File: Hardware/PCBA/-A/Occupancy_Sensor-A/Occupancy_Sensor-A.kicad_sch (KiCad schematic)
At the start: 60 parts, among them J1 USB_C_Receptacle, J2 Conn_02x05_Odd_Even, Q1 2N7002, Q2 2N7002, SW1 SW_Push, SW2 SW_SPDT, U1 TPS78318DDCR, U3 TPS562200, U4 STM32WB55CGUx, U6 ECMF02-2AMX6, Y1 Crystal_GND24_Small, Y2 Crystal_GND24_Small

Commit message: Start layout, component fixes
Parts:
- C1, C10, C11, C12, C13, C14, C15, C16, C17, C18, C19, C2, C20, C21, C22, C23, C24, C25, C3, C4, C5, C6, C7, C8, C9: footprint (none) -> Capacitor_SMD:C_0402_1005Metric
- D2, D3: footprint (none) -> LED_SMD:LED_0603_1608Metric
- J1: footprint (none) -> Connector_USB:USB_C_Receptacle_Molex_105450-0101
- J2: footprint (none) -> Connector_PinHeader_1.27mm:PinHeader_2x05_P1.27mm_Vertical_SMD
- JP1: footprint (none) -> Jumper:SolderJumper-2_P1.3mm_Open_TrianglePad1.0x1.5mm
- L1: footprint (none) -> Inductor_SMD:L_0805_2012Metric
- L2: footprint (none) -> Inductor_SMD:L_Sumida_CDMC6D28_7.25x6.5mm
- L3: footprint (none) -> Inductor_SMD:L_0402_1005Metric
- R1, R2, R3, R4: footprint (none) -> Resistor_SMD:R_0402_1005Metric
- R10, R11, R12, R13, R14, R15, R6, R9: renamed from R5; footprint (none) -> Resistor_SMD:R_0402_1005Metric
- R5: renamed from R8; footprint (none) -> Resistor_SMD:R_0402_1005Metric
- R7: renamed from R6; footprint (none) -> Resistor_SMD:R_0402_1005Metric
- R8: renamed from R7; footprint (none) -> Resistor_SMD:R_0402_1005Metric
- SW1: footprint (none) -> Button_Switch_SMD:SW_Push_SPST_NO_Alps_SKRK
- SW2: footprint (none) -> Button_Switch_SMD:SW_SPDT_CK-JS102011SAQN
- U1: footprint TPS78318DDCR:SOT95P280X110-5N -> Package_TO_SOT_SMD:SOT-23-5
- U2: footprint (none) -> Occupancy_Sensor_Custom_Footprints:TCS3430
- Y1, Y2: footprint (none) -> Crystal:Crystal_SMD_SeikoEpson_FA128-4Pin_2.0x1.6mm
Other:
- moved on the sheet: C1, C10, C11, C12, C13, C14, C15, C16, C18, C19, C2, C20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

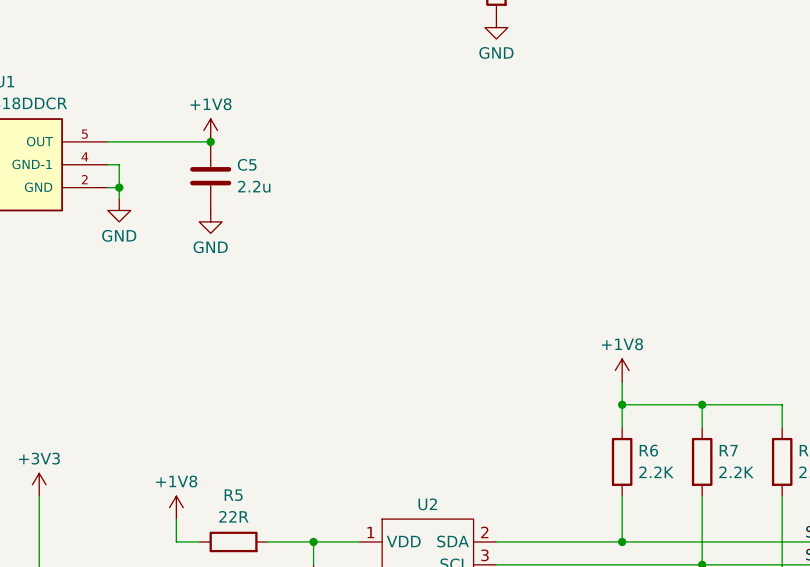
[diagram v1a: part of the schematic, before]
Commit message: Add central custom parts directory
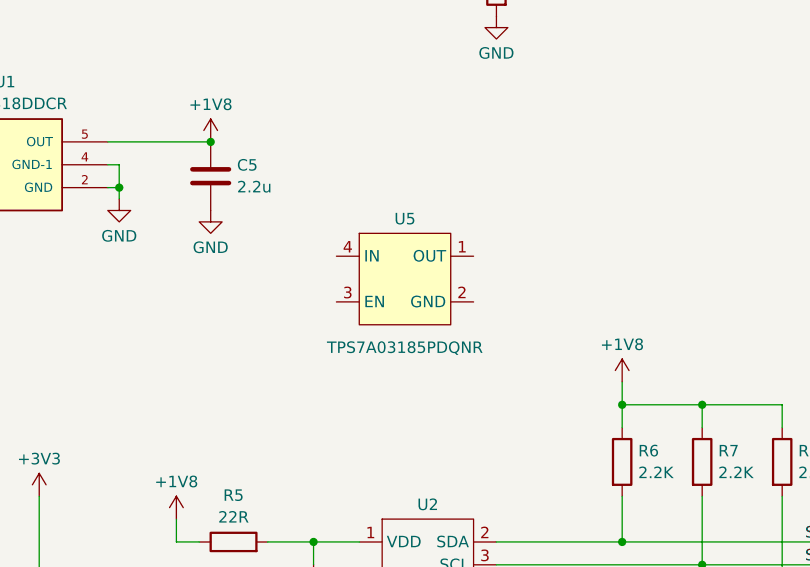
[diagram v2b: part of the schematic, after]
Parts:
- added U5: TPS7A03185PDQNR, symbol Occupancy_Sensor_Custom_Symbols:TPS7A03185PDQNR
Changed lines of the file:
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@@
+    )
+  )
+  (symbol (lib_id "Occupancy_Sensor_Custom_Symbols:TPS7A03185PDQNR") (at 100.33 167.64 0) (unit 1)
+    (in_bom yes) (on_board yes) (dnp no)
+    (property "Reference" "U5" (at 100.33 162.2369 0)
+      (effects (font (size 1.27 1.27)))
+    )
+    (property "Value" "TPS7A03185PDQNR" (at 100.33 176.53 0)
+      (effects (font (size 1.27 1.27)))
+    )
+    (property "Footprint" "" (at 100.33 167.64 0)
+      (effects (font (size 1.27 1.27)) hide)
+    )
+    (property "Datasheet" "" (at 100.33 167.64 0)
+      (effects (font (size 1.27 1.27)) hide)
+    )
+    (pin "1")
+    (pin "2")
+    (pin "3")
+    (pin "4")
+    (instances
+      (project "Occupancy_Sensor-A"
+        (path "/65754ac2-2d88-4eb3-8ab1-1eadbd0f428e"
+          (reference "U5") (unit 1)
+        )
+      )
     )
   )

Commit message: General layout, regulator fixes
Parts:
- removed C19, C20: 22u, Capacitor_SMD:C_0402_1005Metric, symbol Device:C
- removed C21: 10u, Capacitor_SMD:C_0402_1005Metric, symbol Device:C
- removed C22, C23, C24: 100n, Capacitor_SMD:C_0402_1005Metric, symbol Device:C_Small
- removed L2: 3.3u, Inductor_SMD:L_Sumida_CDMC6D28_7.25x6.5mm, symbol Device:L
- removed R10: 10K, Resistor_SMD:R_0402_1005Metric, symbol Device:R
- removed R9: 33.2K, Resistor_SMD:R_0402_1005Metric, symbol Device:R
- removed U1: TPS78318DDCR, Package_TO_SOT_SMD:SOT-23-5, symbol TPS78318DDCR:TPS78318DDCR
- removed U3: TPS562200, Package_TO_SOT_SMD:SOT-23-6, symbol Regulator_Switching:TPS562200
- removed U5: TPS7A03185PDQNR, symbol Occupancy_Sensor_Custom_Symbols:TPS7A03185PDQNR
- added C26: 1u, Capacitor_SMD:C_0402_1005Metric, symbol Device:C
- added U1: TPS7A0333PDBV, Package_TO_SOT_SMD:SOT-23-5, symbol Occupancy_Sensor_Custom_Symbols:TPS7A0333PDBV
- added U3: TPS7A03185PDBV, Package_TO_SOT_SMD:SOT-23-5, symbol Occupancy_Sensor_Custom_Symbols:TPS7A03185PDBV
- C18: value 10u -> 1u
- C5: value 2.2u -> 1u
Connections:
- net +1V8: now also C18.1, U3.5 (OUT); no longer C5.1
- net +3.3V: now also C5.1, U1.5 (OUT); no longer C16.1
- net 1V8_EN: now also U3.3 (EN)
- net GND: now also C26.2, U1.2 (GND), U3.2 (GND)
- net OSC32_IN: now also C15.1
- net OSC32_OUT: no longer C15.1
- net VBUS: now also C16.1, C26.1, U1.1 (IN), U1.3 (EN), U3.1 (IN); no longer C18.1
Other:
- moved on the sheet: C16
